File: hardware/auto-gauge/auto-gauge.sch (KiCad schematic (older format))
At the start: 41 parts

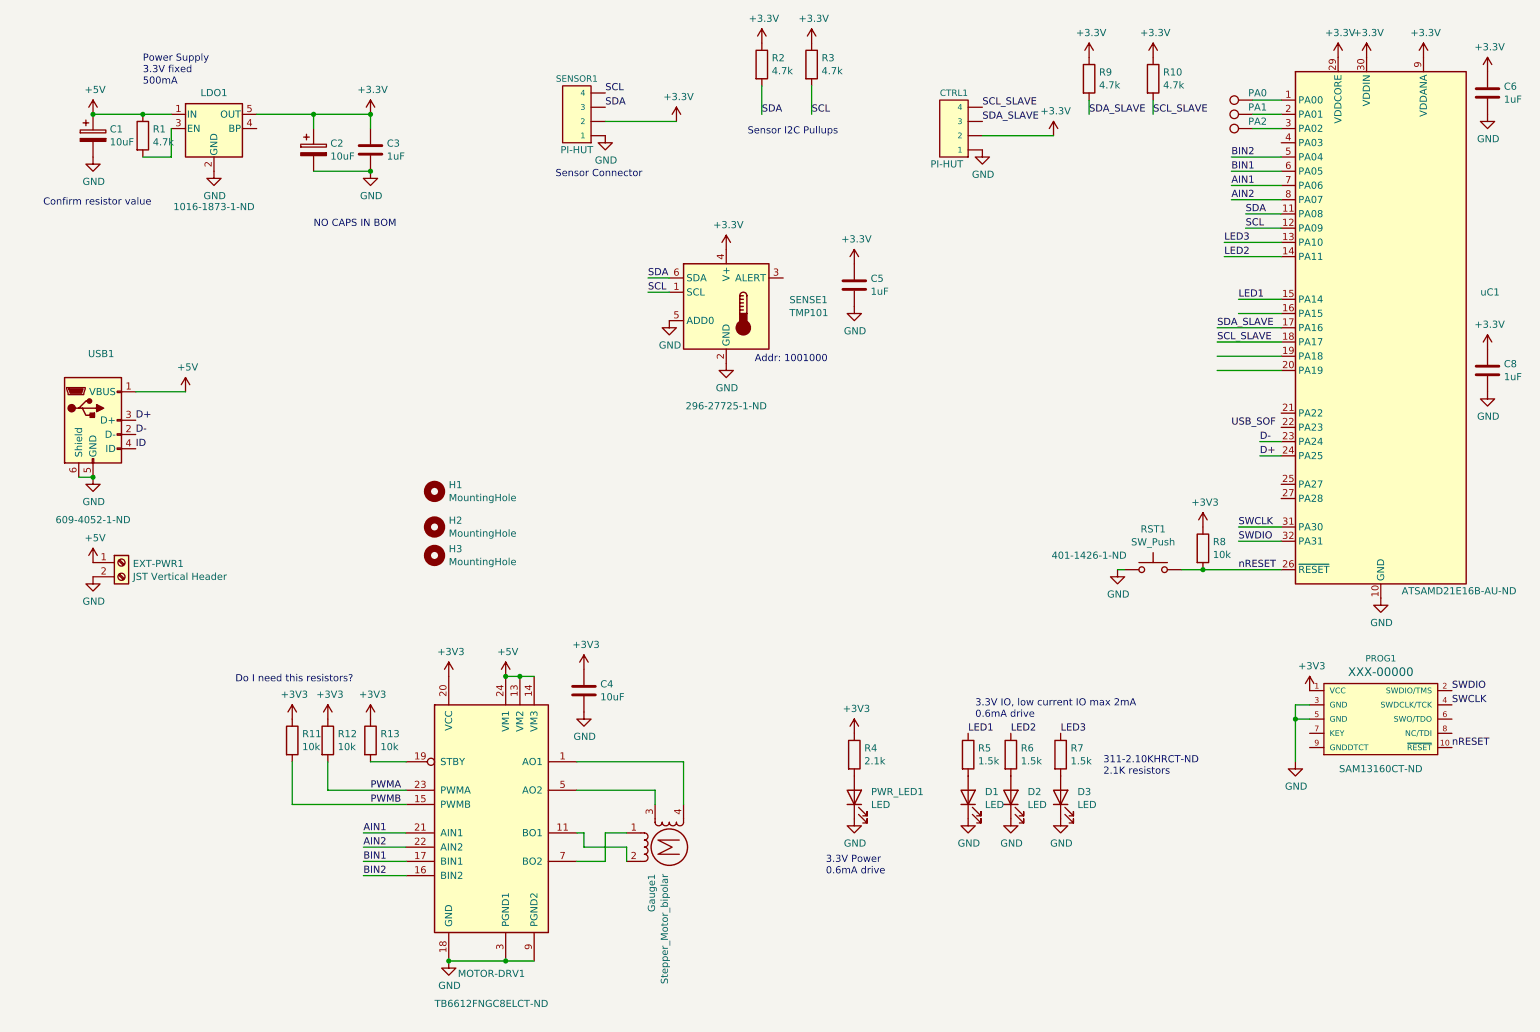
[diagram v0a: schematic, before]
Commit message: arduino dummy/test. New board using atmega328 for jlcpcb asm
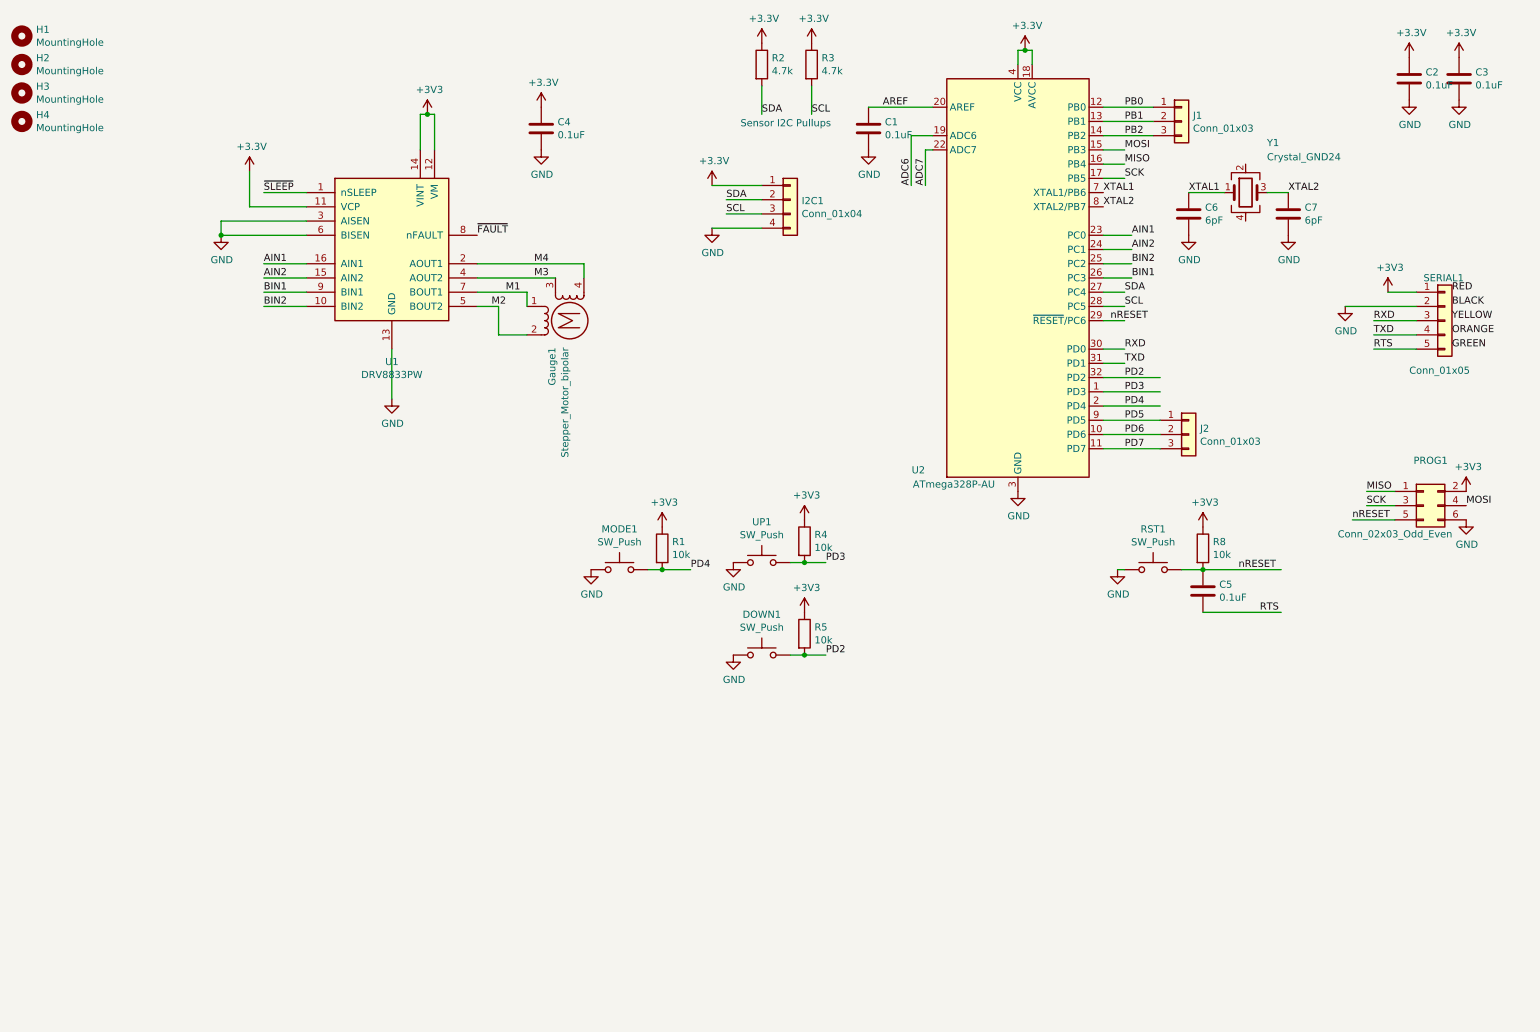
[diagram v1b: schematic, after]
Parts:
- removed C1, C2: 10uF, Capacitor_SMD:C_0603_1608Metric, symbol Device:CP
- removed C4: 10uF, Capacitor_SMD:C_0603_1608Metric, symbol Device:C
- removed CTRL1: CONN_04JST-SH, Connector_JST:JST_SH_BM04B-SRSS-TB_1x04-1MP_P1.00mm_Vertical, symbol SF_CONN:CONN_04JST-PTH
- removed D1, D2, D3, PWR_LED1: LED, LED_SMD:LED_0603_1608Metric, symbol Device:LED
- removed EXT-PWR1: JST Vertical Header, Connector_JST:JST_EH_B2B-EH-A_1x02_P2.50mm_Vertical, symbol Connector:Screw_Terminal_01x02
- removed LDO1: SPX3819M5-L-3-3, Package_TO_SOT_SMD:SOT-23-5, symbol Regulator_Linear:SPX3819M5-L-3-3
- removed MOTOR-DRV1: TB6612FNG, Package_SO:SSOP-24_5.3x8.2mm_P0.65mm, symbol Driver_Motor:TB6612FNG
- removed PA0, PA1, PA2: TestPoint, TestPoint:TestPoint_Pad_1.0x1.0mm, symbol Connector:TestPoint
- removed PROG1: CORTEX_DEBUG_SMD, SAMTECH_FTSH-105-01, symbol SF_CONN:CORTEX_DEBUG_SMD
- removed R10, R9: 4.7k, Resistor_SMD:R_0603_1608Metric, symbol Device:R
- removed R11, R12, R13: 10k, Resistor_SMD:R_0603_1608Metric, symbol Device:R
- removed R6, R7: 1.5k, Resistor_SMD:R_0603_1608Metric, symbol Device:R
- removed SENSE1: TMP101, Package_TO_SOT_SMD:SOT-23-6, symbol Sensor_Temperature:TMP101
- removed SENSOR1: CONN_04JST-PTH, Connector_JST:JST_SH_BM04B-SRSS-TB_1x04-1MP_P1.00mm_Vertical, symbol SF_CONN:CONN_04JST-PTH
- removed USB1: USB_B_Micro, Connector_USB:USB_Micro-B_Amphenol_10104110_Horizontal, symbol Connector:USB_B_Micro
- removed uC1: ATSAMD21E16B-A, Package_QFP:TQFP-32_7x7mm_P0.8mm, symbol MCU_Microchip_SAMD:ATSAMD21E16A-A
- added C1, C2: 0.1uF, Capacitor_SMD:C_0603_1608Metric, symbol Device:C
- added C7: 6pF, Capacitor_SMD:C_0603_1608Metric, symbol Device:C
- added DOWN1, MODE1, UP1: SW_Push, Button_Switch_SMD:SW_SPST_TL3342, symbol Switch:SW_Push
- added H4: MountingHole, MountingHole:MountingHole_2.2mm_M2, symbol Mechanical:MountingHole
- added I2C1: Conn_01x04, Connector_PinHeader_2.54mm:PinHeader_1x04_P2.54mm_Vertical, symbol Connector_Generic:Conn_01x04
- added J1, J2: Conn_01x03, Connector_PinHeader_2.54mm:PinHeader_1x03_P2.54mm_Vertical, symbol Connector_Generic:Conn_01x03
- added PROG1: Conn_02x03_Odd_Even, Connector_PinHeader_2.54mm:PinHeader_2x03_P2.54mm_Vertical, symbol Connector_Generic:Conn_02x03_Odd_Even
- added SERIAL1: Conn_01x05, Connector_PinHeader_2.54mm:PinHeader_1x05_P2.54mm_Vertical, symbol Connector_Generic:Conn_01x05
- added U1: DRV8833PW, Package_SO:TSSOP-16_4.4x5mm_P0.65mm, symbol Driver_Motor:DRV8833PW
- added U2: ATmega328P-AU, Package_QFP:TQFP-32_7x7mm_P0.8mm, symbol MCU_Microchip_ATmega:ATmega328P-AU
- added Y1: Crystal_GND24, Crystal:Crystal_SMD_Abracon_ABM8G-4Pin_3.2x2.5mm, symbol Device:Crystal_GND24
- C3, C5: value 1uF -> 0.1uF; LCSC (none) -> C14663
- C4: renamed from C8; value 1uF -> 0.1uF; LCSC (none) -> C14663
- C6: value 1uF -> 6pF; LCSC (none) -> C37474
- R1: value 4.7k -> 10k; LCSC (none) -> C25197
- R2, R3: LCSC (none) -> C23162; PN 311-4.7KGRCT-ND -> (none)
- R4: value 2.1k -> 10k; LCSC (none) -> C25197
- R5: value 1.5k -> 10k; LCSC (none) -> C25197
- R8: Digi-Key_PN 311-10.0KHRCT-ND -> (none); LCSC (none) -> C25197; PN 311-10.0KHRCT-ND -> (none)
- RST1: footprint Button_Switch_SMD:SW_Push_1P1T-SH_NO_CK_KMR2xxG -> Button_Switch_SMD:SW_SPST_TL3342; Digi-Key_PN 401-1426-1-ND -> (none); LCSC (none) -> C318884; PN 401-1426-1-ND -> (none)
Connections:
- net labels added: ADC6, ADC7, AREF, BLACK, GREEN, M1, M2, M3, M4, MISO, MOSI, ORANGE, PB0, PB1, PB2, PD2, PD3, PD4, PD5, PD6, PD7, RED, RTS, RXD, SCK, TXD, XTAL1, XTAL2, YELLOW, ~FAULT, ~SLEEP
- net labels removed: +5V, D+, D-, ID, LED1, LED2, LED3, PWMA, PWMB, SCL_SLAVE, SDA_SLAVE, SWCLK, SWDIO, USB_SOF
- wire segments 71 -> 79
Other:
- note removed: "3.3V IO, low current IO max 2mA\n0.6mA drive\n"
- note removed: "3.3V Power\n0.6mA drive"
- note removed: "311-2.10KHRCT-ND\n2.1K resistors"
- note removed: "Addr: 1001000"
- note removed: "Confirm resistor value"
- note removed: "Do I need this resistors?"
- note removed: "NO CAPS IN BOM"
- note removed: "Power Supply\n3.3V fixed\n500mA"
- note removed: "Sensor Connector"
- moved on the sheet: C4, Gauge1, H1, H2, H3
